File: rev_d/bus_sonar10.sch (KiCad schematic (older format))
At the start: 40 parts, among them J1 TERMINATE_JUMPER, SW1 MJTP1243, U1 74HCT08, U2 LM2940, U3 MCP2562, U4 ATMEGA328_DIP28, U5 74HCT32, X1 16MHz

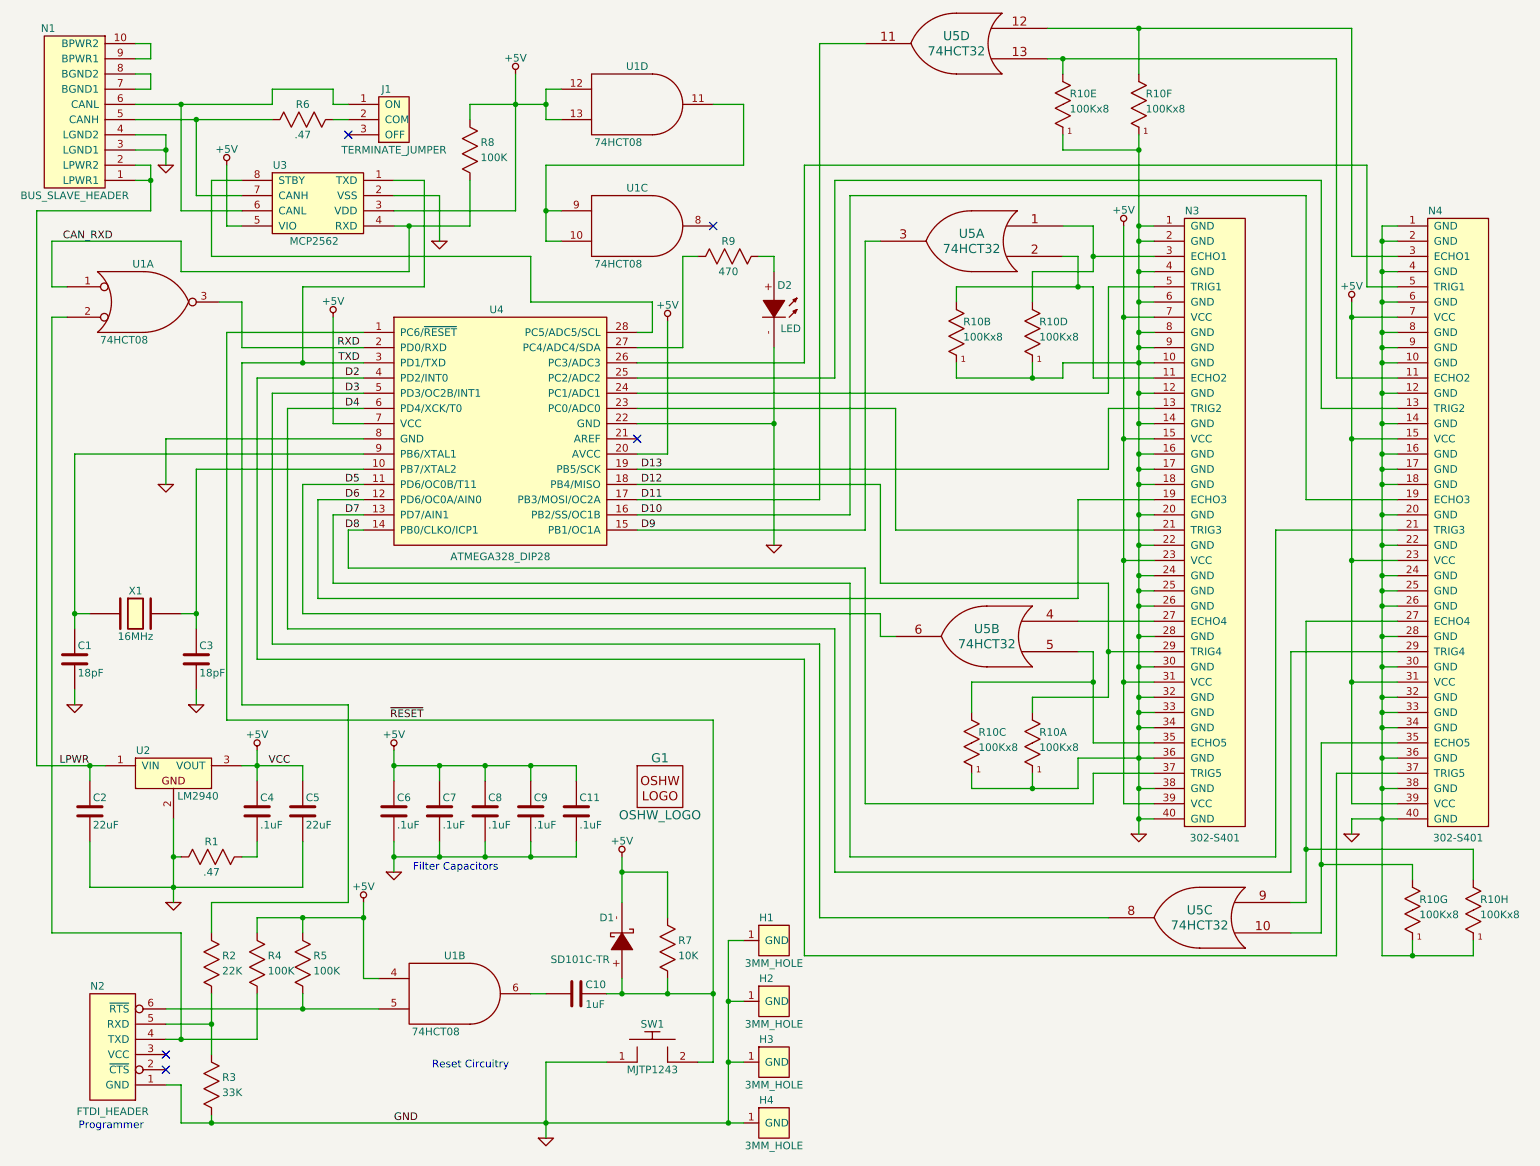
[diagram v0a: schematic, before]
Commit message: Added ISP connector.
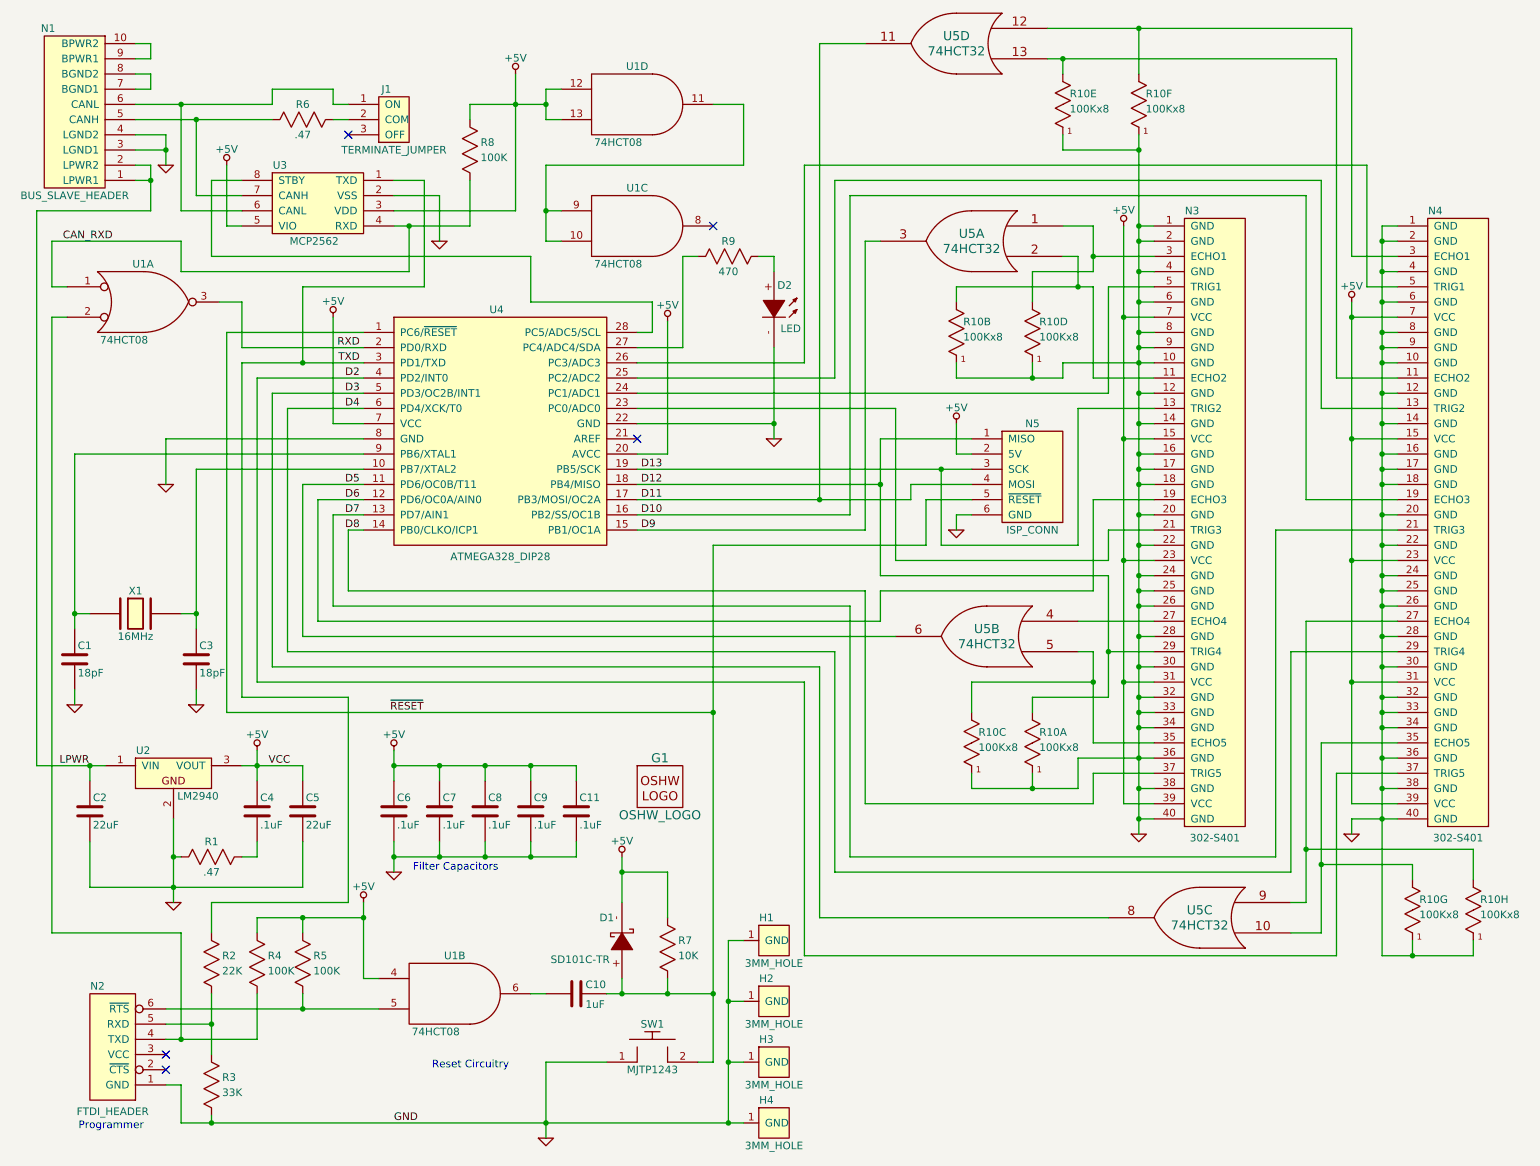
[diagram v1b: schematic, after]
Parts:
- added N5: ISP_CONN, bus_sonar10:Pin_Header_Straight_2x03, symbol ISP_CONN
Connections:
- net +5V: now also N5.2 (5V)
- net D11: now also N5.4 (MOSI)
- net D12: now also N5.1 (MISO)
- net D13: now also N5.3 (SCK)
- net GND: now also N5.6 (GND)
- net ~RESET: now also N5.5 (~RESET)

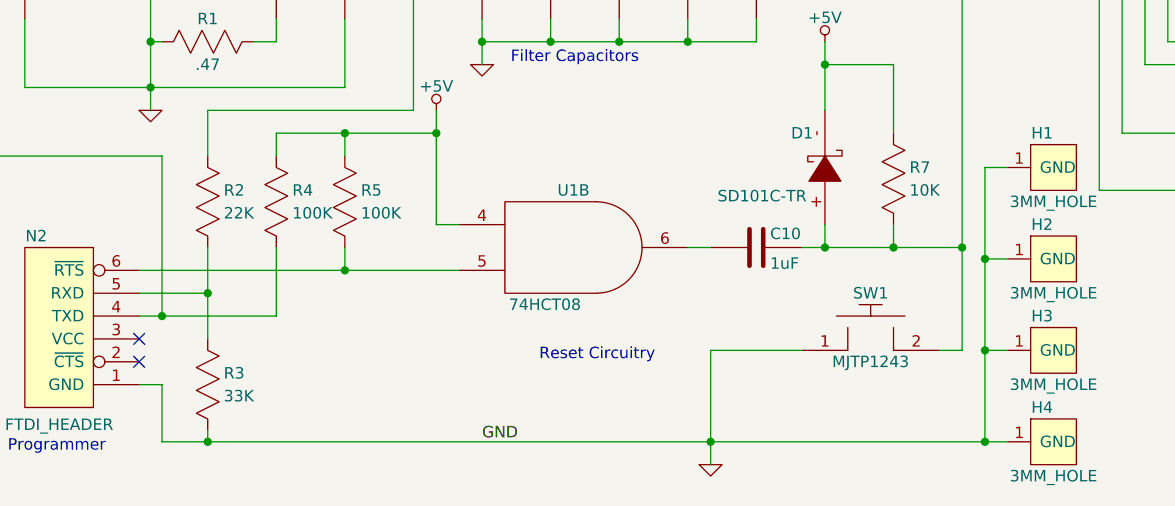
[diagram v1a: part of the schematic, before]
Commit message: Mounting holes are now electrically isolated.
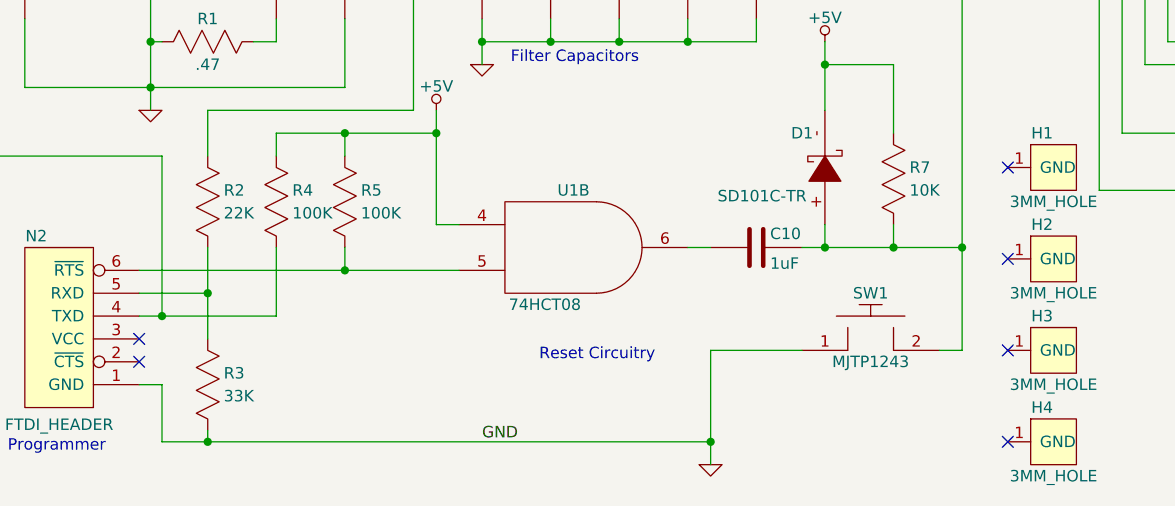
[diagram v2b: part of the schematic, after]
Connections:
- net GND: no longer H1.1 (GND), H2.1 (GND), H3.1 (GND), H4.1 (GND)
- no-connect marks 5 -> 9
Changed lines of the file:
@@
 	1800 6950 1800 7350
-Wire Wire Line
-	1600 7800 5300 7800
 Wire Wire Line
 	1800 7750 1800 7800
@@
 	5100 7400 5000 7400
 Connection ~ 5100 6950
-Wire Wire Line
-	5200 6600 5200 7800
-Wire Wire Line
-	5200 6600 5300 6600
-Wire Wire Line
-	5300 7000 5200 7000
-Connection ~ 5200 7000
-Wire Wire Line
-	5300 7400 5200 7400
-Connection ~ 5200 7400
-Connection ~ 5200 7800
 Wire Wire Line
 	4400 7400 4000 7400
@@
 	6500 3700 6800 3700
 Connection ~ 5100 5100
+NoConn ~ 5300 6600
+NoConn ~ 5300 7000
+NoConn ~ 5300 7400
+NoConn ~ 5300 7800
+Wire Wire Line
+	1600 7800 4000 7800
 $EndSCHEMATC

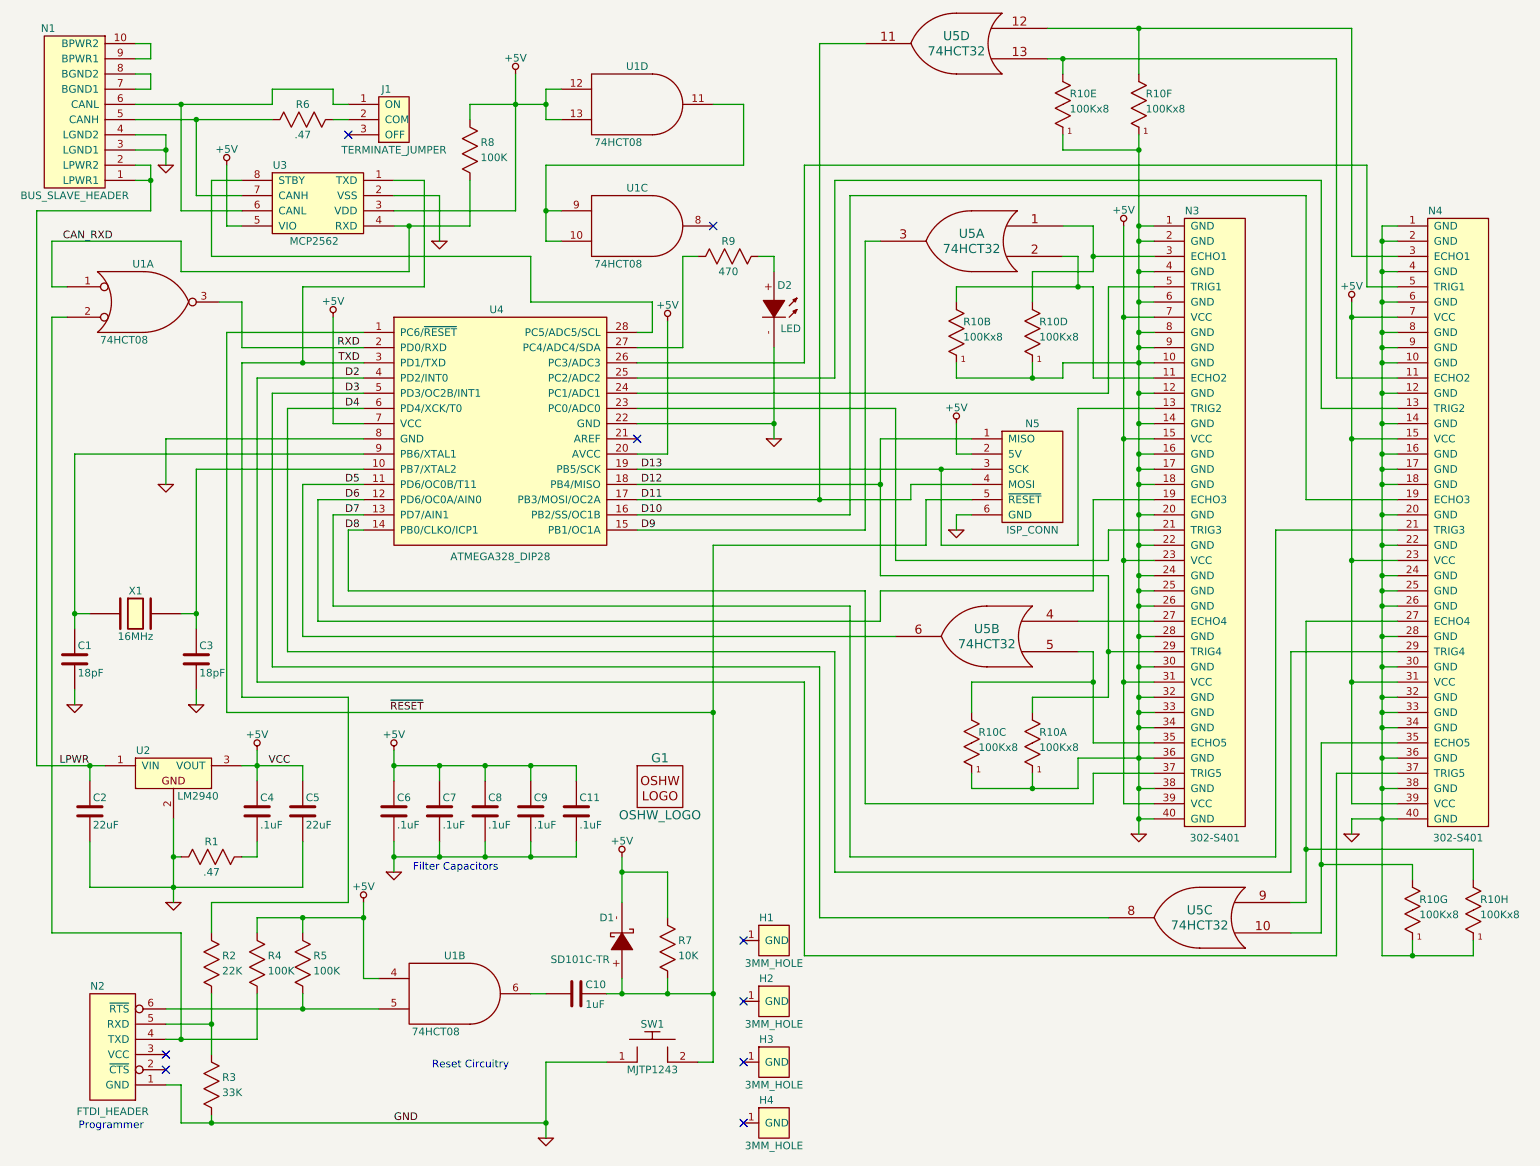
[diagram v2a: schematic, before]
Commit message: Split 22uF capacitor into aluminum and tantalum.
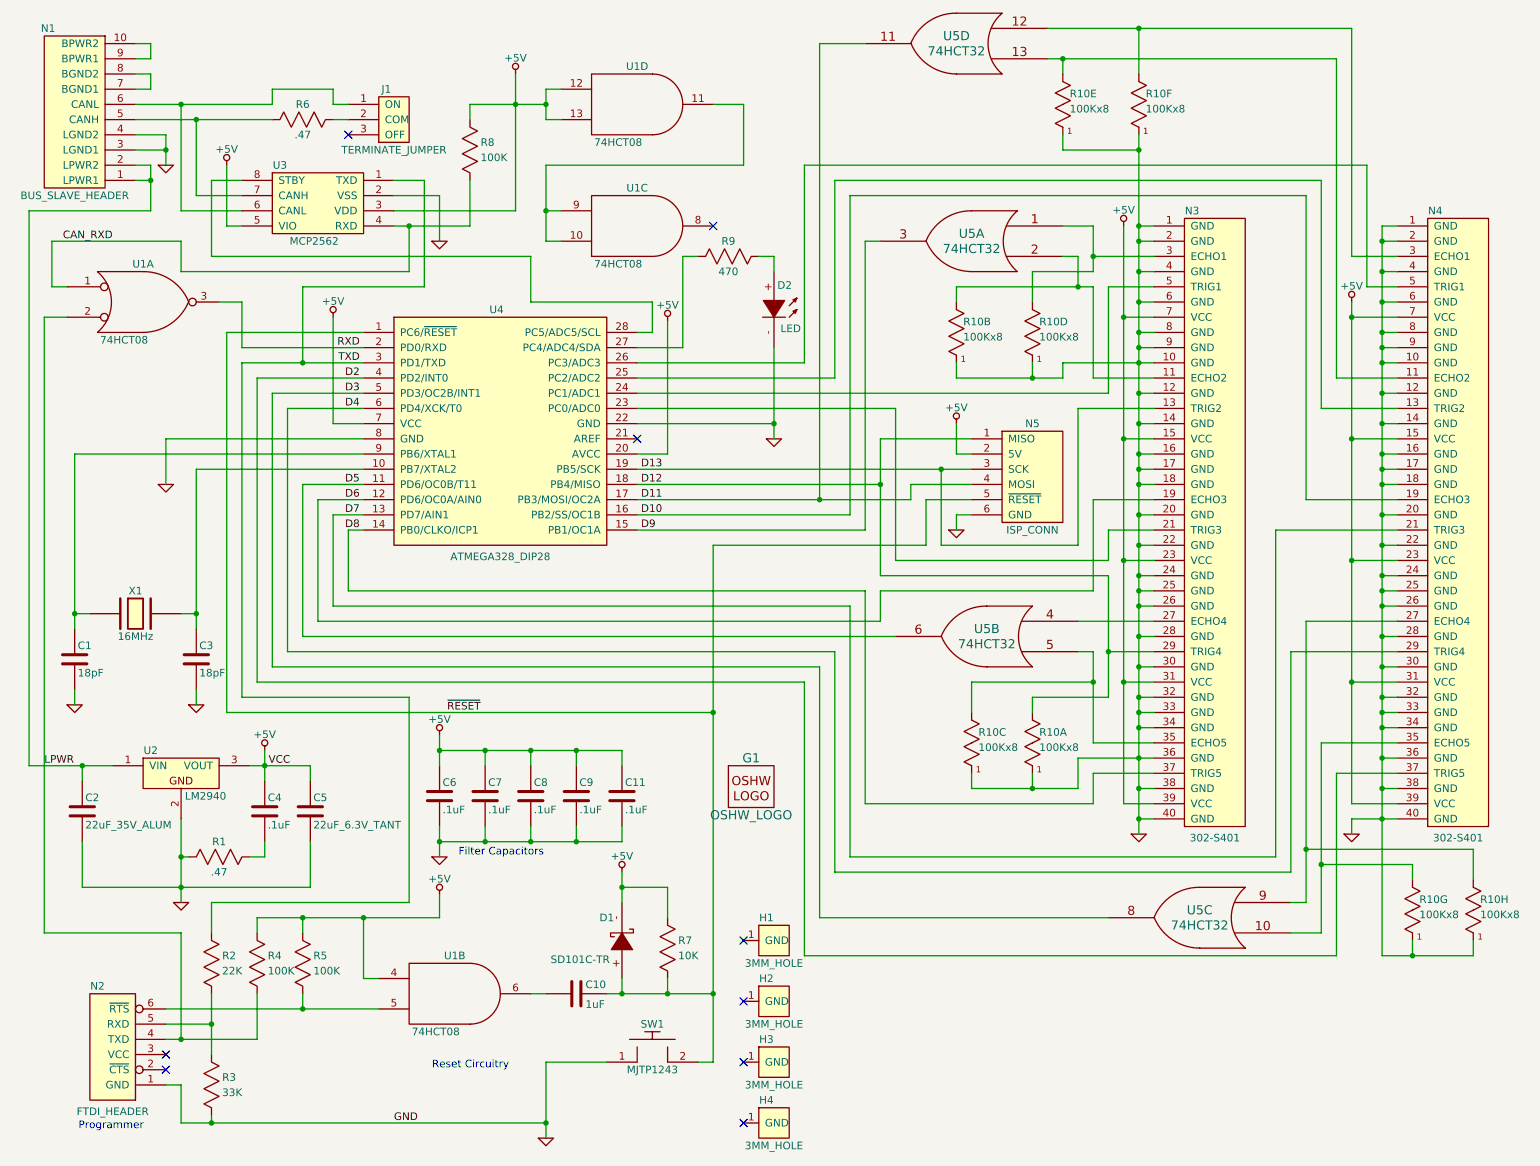
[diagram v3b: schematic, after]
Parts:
- C2: value 22uF -> 22uF_35V_ALUM
- C5: value 22uF -> 22uF_6.3V_TANT
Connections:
- net LPWR: now also N2.4 (TXD), R4.1, U1.2
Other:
- moved on the sheet: C11, C2, C4, C5, C6, C7, C8, C9, G1, R1, U2
